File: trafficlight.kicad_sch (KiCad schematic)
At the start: 7 parts, among them P1 Conn_01x06

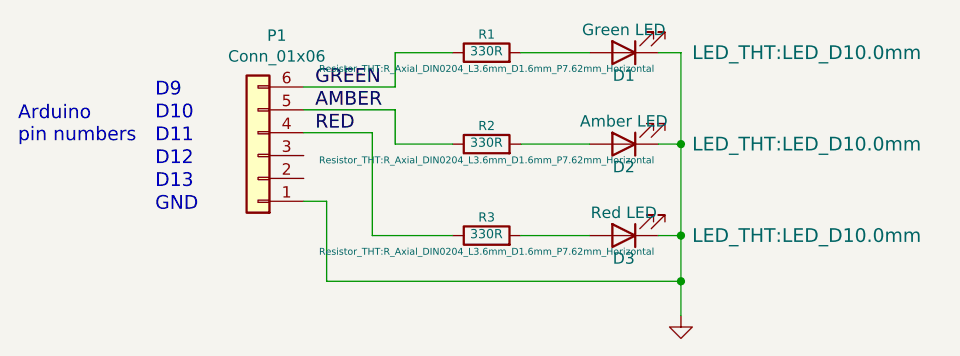
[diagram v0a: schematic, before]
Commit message: Change resistor footprints.
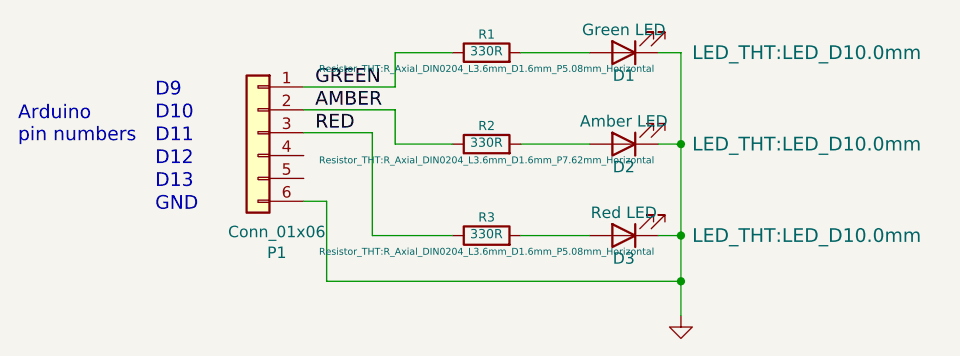
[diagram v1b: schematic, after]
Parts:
- R1, R3: footprint Resistor_THT:R_Axial_DIN0204_L3.6mm_D1.6mm_P7.62mm_Horizontal -> Resistor_THT:R_Axial_DIN0204_L3.6mm_D1.6mm_P5.08mm_Horizontal
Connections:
- net AMBER: now also P1.2 (Pin_2); no longer P1.5 (Pin_5)
- net GND: now also P1.6 (Pin_6); no longer P1.1 (Pin_1)
- net GREEN: now also P1.1 (Pin_1); no longer P1.6 (Pin_6)
- net RED: now also P1.3 (Pin_3); no longer P1.4 (Pin_4)
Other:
- moved on the sheet: P1
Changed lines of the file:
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@@
+    (stroke (width 0) (type default) (color 0 0 0 0))
+  )
+  (wire (pts (xy 113.03 93.98) (xy 120.65 93.98))
+    (stroke (width 0) (type default) (color 0 0 0 0))
+  )
+  (wire (pts (xy 88.9 77.47) (xy 99.06 77.47))
+    (stroke (width 0) (type default) (color 0 0 0 0))
+  )
+  (wire (pts (xy 99.06 83.82) (xy 105.41 83.82))
+    (stroke (width 0) (type default) (color 0 0 0 0))
+  )
+  (wire (pts (xy 128.27 83.82) (xy 130.81 83.82))
     (stroke (width 0) (type default) (color 0 0 0 0))
   )
@@
     (stroke (width 0) (type default) (color 0 0 0 0))
   )
-  (wire (pts (xy 113.03 93.98) (xy 120.65 93.98))
-    (stroke (width 0) (type default) (color 0 0 0 0))
-  )
-  (wire (pts (xy 88.9 77.47) (xy 99.06 77.47))
-    (stroke (width 0) (type default) (color 0 0 0 0))
-  )
-  (wire (pts (xy 99.06 83.82) (xy 105.41 83.82))
-    (stroke (width 0) (type default) (color 0 0 0 0))
-  )
-  (wire (pts (xy 128.27 83.82) (xy 130.81 83.82))
-    (stroke (width 0) (type default) (color 0 0 0 0))
-  )
   (wire (pts (xy 91.44 99.06) (xy 130.81 99.06))
     (stroke (width 0) (type default) (color 0 0 0 0))
@@
     (stroke (width 0) (type default) (color 0 0 0 0))
   )
+  (wire (pts (xy 88.9 80.01) (xy 99.06 80.01))
+    (stroke (width 0) (type default) (color 0 0 0 0))
+  )
   (wire (pts (xy 128.27 93.98) (xy 130.81 93.98))
     (stroke (width 0) (type default) (color 0 0 0 0))
@@
     (stroke (width 0) (type default) (color 0 0 0 0))
   )
+  (wire (pts (xy 88.9 82.55) (xy 96.52 82.55))
+    (stroke (width 0) (type default) (color 0 0 0 0))
+  )
   (wire (pts (xy 130.81 73.66) (xy 130.81 83.82))
     (stroke (width 0) (type default) (color 0 0 0 0))
   )
-  (wire (pts (xy 88.9 82.55) (xy 96.52 82.55))
-    (stroke (width 0) (type default) (color 0 0 0 0))
-  )
   (wire (pts (xy 130.81 83.82) (xy 130.81 93.98))
     (stroke (width 0) (type default) (color 0 0 0 0))
@@
     (stroke (width 0) (type default) (color 0 0 0 0))
   )
-  (wire (pts (xy 88.9 80.01) (xy 99.06 80.01))
-    (stroke (width 0) (type default) (color 0 0 0 0))
-  )
   (text "D13" (at 72.39 88.9 0)
     (effects (font (size 1.524 1.524)) (justify left bottom))
@@
       (effects (font (size 1.016 1.016)))
     )
-    (property "Footprint" "Resistor_THT:R_Axial_DIN0204_L3.6mm_D1.6mm_P7.62mm_Horizontal" (id 2) (at 109.22 75.438 90)
+    (property "Footprint" "Resistor_THT:R_Axial_DIN0204_L3.6mm_D1.6mm_P5.08mm_Horizontal" (id 2) (at 109.22 75.438 90)
       (effects (font (size 0.762 0.762)))
     )
@@
       (effects (font (size 1.016 1.016)))
     )
-    (property "Footprint" "Resistor_THT:R_Axial_DIN0204_L3.6mm_D1.6mm_P7.62mm_Horizontal" (id 2) (at 109.22 95.758 90)
+    (property "Footprint" "Resistor_THT:R_Axial_DIN0204_L3.6mm_D1.6mm_P5.08mm_Horizontal" (id 2) (at 109.22 95.758 90)
       (effects (font (size 0.762 0.762)))
     )
@@
     (pin "1")
   )
-  (symbol (lib_id "Connector_Generic:Conn_01x06") (at 83.82 85.09 180) (unit 1)
-    (in_bom yes) (on_board yes)
-    (property "Reference" "P1" (id 0) (at 85.9028 71.755 0))
-    (property "Value" "Conn_01x06" (id 1) (at 85.9028 74.0664 0))
-    (property "Footprint" "Connector_PinHeader_2.54mm:PinHeader_1x06_P2.54mm_Horizontal" (id 2) (at 83.82 85.09 0)
+  (symbol (lib_id "Connector_Generic:Conn_01x06") (at 83.82 82.55 0) (mirror y) (unit 1)
+    (in_bom yes) (on_board yes)
+    (property "Reference" "P1" (id 0) (at 85.9028 95.885 0))
+    (property "Value" "Conn_01x06" (id 1) (at 85.9028 93.5736 0))
+    (property "Footprint" "Connector_PinHeader_2.54mm:PinHeader_1x06_P2.54mm_Horizontal" (id 2) (at 83.82 82.55 0)
       (effects (font (size 1.27 1.27)) hide)
     )
-    (property "Datasheet" "~" (id 3) (at 83.82 85.09 0)
+    (property "Datasheet" "~" (id 3) (at 83.82 82.55 0)
       (effects (font (size 1.27 1.27)) hide)
     )
@@
     )
     (path "/00000000-0000-0000-0000-000055ab6e54"
-      (reference "R1") (unit 1) (value "330R") (footprint "Resistor_THT:R_Axial_DIN0204_L3.6mm_D1.6mm_P7.62mm_Horizontal")
+      (reference "R1") (unit 1) (value "330R") (footprint "Resistor_THT:R_Axial_DIN0204_L3.6mm_D1.6mm_P5.08mm_Horizontal")
     )
     (path "/00000000-0000-0000-0000-000055ab6e63"
@@
     )
     (path "/00000000-0000-0000-0000-000055ab6e72"
-      (reference "R3") (unit 1) (value "330R") (footprint "Resistor_THT:R_Axial_DIN0204_L3.6mm_D1.6mm_P7.62mm_Horizontal")
-    )
-  )
+      (reference "R3") (unit 1) (value "330R") (footprint "Resistor_THT:R_Axial_DIN0204_L3.6mm_D1.6mm_P5.08mm_Horizontal")
+    )
+  )
